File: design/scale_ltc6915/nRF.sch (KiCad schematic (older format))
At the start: 31 parts, among them J1 USB_B_Micro, J2 Conn_02x03_Odd_Even, J4 Conn_01x04, Q1 IRLML6401, SW1 SW_SPST, SW2 ON/OFF switch, U1 MDBT42Q, U2 BQ21040, U3 TPS7A0233PDBV, Y1 Q13FC1350000400

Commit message: BOMs, schematics updated, scale_ltc6915 PCB Design complete.
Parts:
- added Q3: AO3400, Package_TO_SOT_SMD:SOT-23, symbol Device:Q_NMOS_DGS
- added R10, R11: 10k, Resistor_SMD:R_0603_1608Metric_Pad1.05x0.95mm_HandSolder, symbol sense:R
- J4: footprint Connector_PinHeader_2.00mm:PinHeader_1x04_P2.00mm_Vertical -> Connector_PinHeader_2.00mm:PinHeader_1x02_P2.00mm_Vertical; symbol Connector_Generic:Conn_01x04 -> Connector_Generic:Conn_01x02
- U3: symbol scale_ltc6915.pro-rescue:TLV70013_SOT23-5-Regulator_Linear -> scale_ltc6915-rescue:TLV70013_SOT23-5-Regulator_Linear
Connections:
- net 10V_LDO_EN: now also U1.23 (P0.10/NFC2); no longer U1.16 (P0.03/AIN1)
- net BOOST_EN: now also U1.22 (P0.09/NFC1); no longer U1.17 (P0.04/AIN2)
- net BUTTON: now also U1.28 (TRACE_DATA3/P0.14); no longer U1.19 (P0.06)
- net CLK_nRF: now also U1.33 (P0.19); no longer U1.25 (P0.11)
- net CS1_nRF: now also U1.31 (P0.17); no longer U1.26 (P0.12)
- net CS2_nRF: now also U1.26 (P0.12); no longer U1.29 (TRACE_DATA2/P0.15)
- net EN_nRF: now also U1.29 (TRACE_DATA2/P0.15); no longer U1.21 (P0.08)
- net GND: now also Q3.3 (S)
- net GPIO0: now also U1.19 (P0.06); no longer U1.33 (P0.19)
- net GPIO1: now also U1.20 (P0.07); no longer U1.32 (TRACE_DATA0/P0.18)
- net MISO_nRF: now also U1.27 (P0.13); no longer U1.28 (TRACE_DATA3/P0.14)
- net MOSI_nRF: now also U1.32 (TRACE_DATA0/P0.18); no longer U1.20 (P0.07)
- net SHDW_nRF: now also U1.30 (TRACE_DATA1/P0.16); no longer U1.27 (P0.13)
- net VBAT: now also R10.2
- net Vlc: now also U1.17 (P0.04/AIN2); no longer U1.18 (P0.05/AIN3)
- removed net GPIO2: J4.3 (Pin_3), U1.31 (P0.17)
- removed net GPIO3: J4.4 (Pin_4), U1.30 (TRACE_DATA1/P0.16)
- new net: Q3.1 (D), R11.1
- new net BAT_LVL: R10.1, R11.2, U1.18 (P0.05/AIN3)
- new net BT_LVL_EN: Q3.2 (G), U1.21 (P0.08)
- no-connect marks 13 -> 12
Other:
- moved on the sheet: C16, SW1
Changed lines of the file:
@@
 L sense:GND #PWR01
 U 1 1 5A8704B4
-P 8770 3120
-F 0 "#PWR01" H 8770 2870 50  0001 C CNN
-F 1 "GND" H 8770 2970 50  0000 C CNN
-F 2 "" H 8770 3120 60  0000 C CNN
-F 3 "" H 8770 3120 60  0000 C CNN
-	1    8770 3120
+P 9320 5800
+F 0 "#PWR01" H 9320 5550 50  0001 C CNN
+F 1 "GND" H 9320 5650 50  0000 C CNN
+F 2 "" H 9320 5800 60  0000 C CNN
+F 3 "" H 9320 5800 60  0000 C CNN
+	1    9320 5800
 	1    0    0    -1
 $EndComp
@@
 Text Notes 6450 1100 0    60   ~ 0
 Reverse polarity protection
-Text Notes 8760 2445 0    60   ~ 0
+Text Notes 9310 5125 0    60   ~ 0
 Button for Tare
 Text Notes 1180 3310 0    60   ~ 0
@@
 L sense:C C16
 U 1 1 5D422270
-P 9510 2900
-F 0 "C16" H 9360 2995 50  0000 L CNN
-F 1 "0.1nF" H 9265 2820 50  0000 L CNN
-F 2 "sense_fp:C_0402_1005Metric" H 9548 2750 30  0001 C CNN
-F 3 "" H 9510 2900 60  0000 C CNN
-	1    9510 2900
+P 10060 5580
+F 0 "C16" H 9910 5675 50  0000 L CNN
+F 1 "0.1nF" H 9815 5500 50  0000 L CNN
+F 2 "sense_fp:C_0402_1005Metric" H 10098 5430 30  0001 C CNN
+F 3 "" H 10060 5580 60  0000 C CNN
+	1    10060 5580
 	-1   0    0    1
 $EndComp
@@
 L sense:GND #PWR032
 U 1 1 5D42FC1A
-P 9510 3110
-F 0 "#PWR032" H 9510 2860 50  0001 C CNN
-F 1 "GND" H 9510 2960 50  0000 C CNN
-F 2 "" H 9510 3110 60  0000 C CNN
-F 3 "" H 9510 3110 60  0000 C CNN
-	1    9510 3110
+P 10060 5790
+F 0 "#PWR032" H 10060 5540 50  0001 C CNN
+F 1 "GND" H 10060 5640 50  0000 C CNN
+F 2 "" H 10060 5790 60  0000 C CNN
+F 3 "" H 10060 5790 60  0000 C CNN
+	1    10060 5790
 	1    0    0    -1
 $EndComp
@@
 L sense:SW_SPST SW1
 U 1 1 5E71D3F6
-P 9160 2640
-F 0 "SW1" H 9160 2765 50  0000 C CNN
-F 1 "SW_SPST" H 9160 2540 50  0000 C CNN
-F 2 "Footprint_nrf_scale:SMD Tactile Switch_3x6x2.5mm" H 9160 2640 50  0001 C CNN
-F 3 "" H 9160 2640 50  0001 C CNN
-	1    9160 2640
+P 9710 5320
+F 0 "SW1" H 9710 5445 50  0000 C CNN
+F 1 "SW_SPST" H 9710 5220 50  0000 C CNN
+F 2 "Footprint_nrf_scale:SMD Tactile Switch_3x6x2.5mm" H 9710 5320 50  0001 C CNN
+F 3 "" H 9710 5320 50  0001 C CNN
+	1    9710 5320
 	1    0    0    -1
 $EndComp
@@
 Wire Wire Line
 	7220 4000 7800 4000
-Text Label 10150 2640 2    50   ~ 0
+Text Label 10700 5320 2    50   ~ 0
 BUTTON
 Wire Wire Line
-	9510 3050 9510 3110
-Wire Wire Line
-	8770 3120 8770 2640
-Wire Wire Line
-	8770 2640 8960 2640
-Wire Wire Line
-	9360 2640 9510 2640
-Wire Wire Line
-	9510 2750 9510 2640
-Connection ~ 9510 2640
-Wire Wire Line
-	9510 2640 10150 2640
+	10060 5730 10060 5790
+Wire Wire Line
+	9320 5800 9320 5320
+Wire Wire Line
+	9320 5320 9510 5320
+Wire Wire Line
+	9910 5320 10060 5320
+Wire Wire Line
+	10060 5430 10060 5320
+Connection ~ 10060 5320
+Wire Wire Line
+	10060 5320 10700 5320
 $Comp
 L sense:Battery_Cell BT1
@@
 VBAT
 $Comp
-L scale_ltc6915.pro-rescue:TLV70013_SOT23-5-Regulator_Linear U?
+L scale_ltc6915-rescue:TLV70013_SOT23-5-Regulator_Linear U?
 U 1 1 5E60E4CD
 P 9300 1450
@@
 Text HLabel 7550 1350 2    50   Output ~ 0
 VBAT
-Text Label 6120 6300 1    50   ~ 0
+Text Label 7800 4600 2    50   ~ 0
 BUTTON
 Wire Wire Line
-	6020 6300 6020 5650
-Wire Wire Line
-	6120 5650 6120 6300
-NoConn ~ 6420 5650
-NoConn ~ 6520 5650
+	6220 6300 6220 5650
+Wire Wire Line
+	6320 5650 6320 6300
 Wire Wire Line
 	7800 4900 7220 4900
@@
 NoConn ~ 5720 5650
 Wire Wire Line
-	6220 5650 6220 6300
-Wire Wire Line
-	6320 5650 6320 6300
+	6420 5650 6420 6300
+Wire Wire Line
+	6520 5650 6520 6300
 NoConn ~ 7220 3600
 $Comp
-L Connector_Generic:Conn_01x04 J4
+L Connector_Generic:Conn_01x02 J4
 U 1 1 5E6691E5
-P 10400 4450
-F 0 "J4" H 10480 4442 50  0000 L CNN
-F 1 "Conn_01x04" H 10480 4351 50  0000 L CNN
-F 2 "Connector_PinHeader_2.00mm:PinHeader_1x04_P2.00mm_Vertical" H 10400 4450 50  0001 C CNN
-F 3 "~" H 10400 4450 50  0001 C CNN
-	1    10400 4450
-	1    0    0    -1
-$EndComp
-Text Label 9900 4350 0    50   ~ 0
+P 10360 4100
+F 0 "J4" H 10440 4092 50  0000 L CNN
+F 1 "Conn_01x04" H 10440 4001 50  0000 L CNN
+F 2 "Connector_PinHeader_2.00mm:PinHeader_1x02_P2.00mm_Vertical" H 10360 4100 50  0001 C CNN
+F 3 "~" H 10360 4100 50  0001 C CNN
+	1    10360 4100
+	1    0    0    -1
+$EndComp
+Text Label 9860 4100 0    50   ~ 0
 GPIO0
-Text Label 9900 4450 0    50   ~ 0
+Text Label 9860 4200 0    50   ~ 0
 GPIO1
-Text Label 9900 4550 0    50   ~ 0
-GPIO2
-Text Label 9900 4650 0    50   ~ 0
-GPIO3
-Wire Wire Line
-	9900 4650 10200 4650
-Wire Wire Line
-	10200 4550 9900 4550
-Wire Wire Line
-	9900 4450 10200 4450
-Wire Wire Line
-	10200 4350 9900 4350
-Text Label 7800 4100 2    50   ~ 0
+Wire Wire Line
+	9860 4200 10160 4200
+Wire Wire Line
+	10160 4100 9860 4100
+Text Label 6120 6300 1    50   ~ 0
 GPIO0
-Text Label 7800 4200 2    50   ~ 0
+Text Label 6220 6300 1    50   ~ 0
 GPIO1
-Text Label 7800 4300 2    50   ~ 0
-GPIO2
-Text Label 7800 4400 2    50   ~ 0
-GPIO3
 Wire Wire Line
 	7220 4400 7800 4400
@@
 Wire Wire Line
 	7800 4300 7220 4300
-Text HLabel 5920 6300 3    50   Output ~ 0
+Text HLabel 6420 6300 3    50   Output ~ 0
 BOOST_EN
-Text HLabel 5820 6300 3    50   Output ~ 0
+Text HLabel 6520 6300 3    50   Output ~ 0
 10V_LDO_EN
-Text HLabel 6020 6300 3    50   Input ~ 0
+Text HLabel 5920 6300 3    50   Input ~ 0
 Vlc
+Text HLabel 7800 4400 2    50   Output ~ 0
+SHDW_nRF
+Text HLabel 7800 4300 2    50   Output ~ 0
+CS1_nRF
+Text HLabel 7800 4200 2    50   Output ~ 0
+MOSI_nRF
+Text HLabel 7800 4100 2    50   Output ~ 0
+CLK_nRF
+Text HLabel 7800 4800 2    50   Output ~ 0
+CS2_nRF
 Text HLabel 7800 4700 2    50   Output ~ 0
-SHDW_nRF
-Text HLabel 7800 4800 2    50   Output ~ 0
-CS1_nRF
-Text HLabel 6220 6300 3    50   Output ~ 0
-MOSI_nRF
-Text HLabel 7800 4900 2    50   Output ~ 0
-CLK_nRF
+MISO_nRF
 Text HLabel 7800 4500 2    50   Output ~ 0
-CS2_nRF
-Text HLabel 7800 4600 2    50   Output ~ 0
-MISO_nRF
-Text HLabel 6320 6300 3    50   Output ~ 0
 EN_nRF
 Wire Wire Line
-	5820 6300 5820 5650
+	6020 6300 6020 5650
+Wire Wire Line
+	6120 5650 6120 6300
+Wire Wire Line
+	7800 4500 7220 4500
+Wire Wire Line
+	7220 4600 7800 4600
+Text Label 10440 2110 2    50   ~ 0
+VBAT
+$Comp
+L Device:Q_NMOS_DGS Q3
+U 1 1 5E6E2B83
+P 10340 3310
+F 0 "Q3" H 10544 3356 50  0000 L CNN
+F 1 "AO3400" H 10544 3265 50  0000 L CNN
+F 2 "Package_TO_SOT_SMD:SOT-23" H 10540 3410 50  0001 C CNN
+F 3 "~" H 10340 3310 50  0001 C CNN
+	1    10340 3310
+	1    0    0    -1
+$EndComp
+$Comp
+L sense:R R10
+U 1 1 5E6E3BA3
+P 10440 2350
+F 0 "R10" V 10340 2350 50  0000 C CNN
+F 1 "10k" V 10440 2350 50  0000 C CNN
+F 2 "Resistor_SMD:R_0603_1608Metric_Pad1.05x0.95mm_HandSolder" V 10370 2350 50  0001 C CNN
+F 3 "" H 10440 2350 50  0001 C CNN
+	1    10440 2350
+	-1   0    0    1
+$EndComp
+$Comp
+L sense:R R11
+U 1 1 5E6E57D8
+P 10440 2860
+F 0 "R11" V 10340 2860 50  0000 C CNN
+F 1 "10k" V 10440 2860 50  0000 C CNN
+F 2 "Resistor_SMD:R_0603_1608Metric_Pad1.05x0.95mm_HandSolder" V 10370 2860 50  0001 C CNN
+F 3 "" H 10440 2860 50  0001 C CNN
+	1    10440 2860
+	-1   0    0    1
+$EndComp
+$Comp
+L sense:GND #PWR0128
+U 1 1 5E6F8C54
+P 10440 3620
+F 0 "#PWR0128" H 10440 3370 50  0001 C CNN
+F 1 "GND" H 10440 3470 50  0000 C CNN
+F 2 "" H 10440 3620 60  0000 C CNN
+F 3 "" H 10440 3620 60  0000 C CNN
+	1    10440 3620
+	1    0    0    -1
+$EndComp
+Wire Wire Line
+	10440 3620 10440 3510
+Wire Wire Line
+	10440 3010 10440 3110
+Wire Wire Line
+	10440 2500 10440 2600
+Wire Wire Line
+	10440 2110 10440 2200
+Wire Wire Line
+	10140 3310 9750 3310
+Wire Wire Line
+	10440 2600 9750 2600
+Connection ~ 10440 2600
+Wire Wire Line
+	10440 2600 10440 2710
+Text Label 9750 2600 0    50   ~ 0
+BAT_LVL
+Text Label 9750 3310 0    50   ~ 0
+BT_LVL_EN
+Text Label 6020 6300 1    50   ~ 0
+BAT_LVL
+Text Label 6320 6300 1    50   ~ 0
+BT_LVL_EN
 Wire Wire Line
 	5920 5650 5920 6300
-Wire Wire Line
-	7800 4500 7220 4500
-Wire Wire Line
-	7220 4600 7800 4600
+NoConn ~ 5820 5650
 $EndSCHEMATC

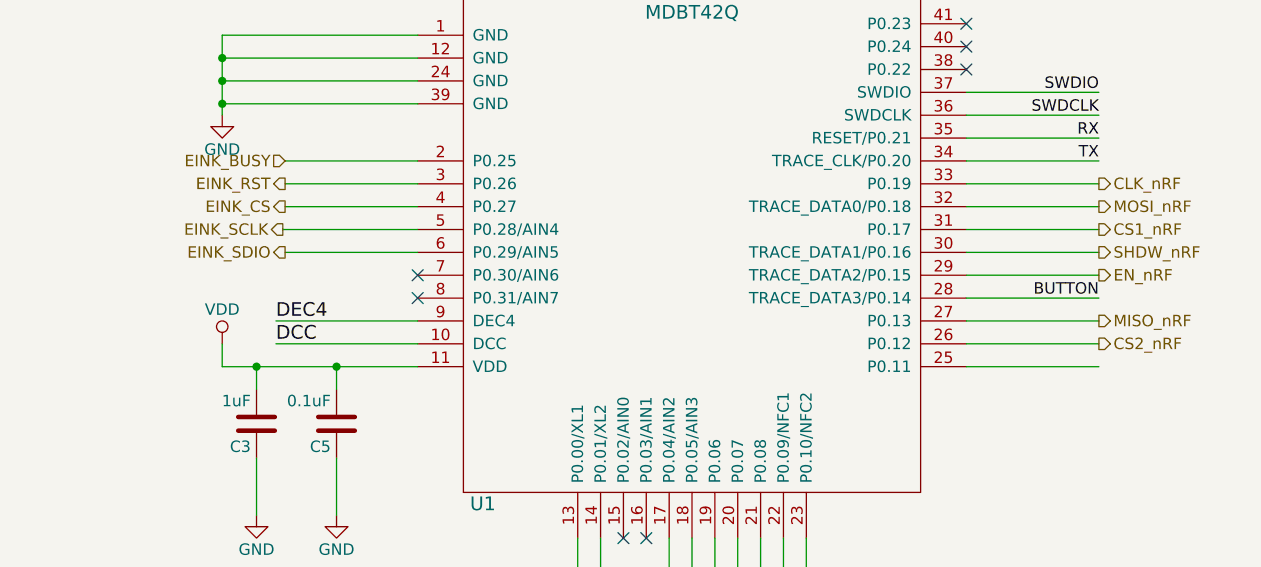
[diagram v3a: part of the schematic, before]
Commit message: DC, CS pins separated, issue fixed. In both scale_hx711 and scale_ltc6915.
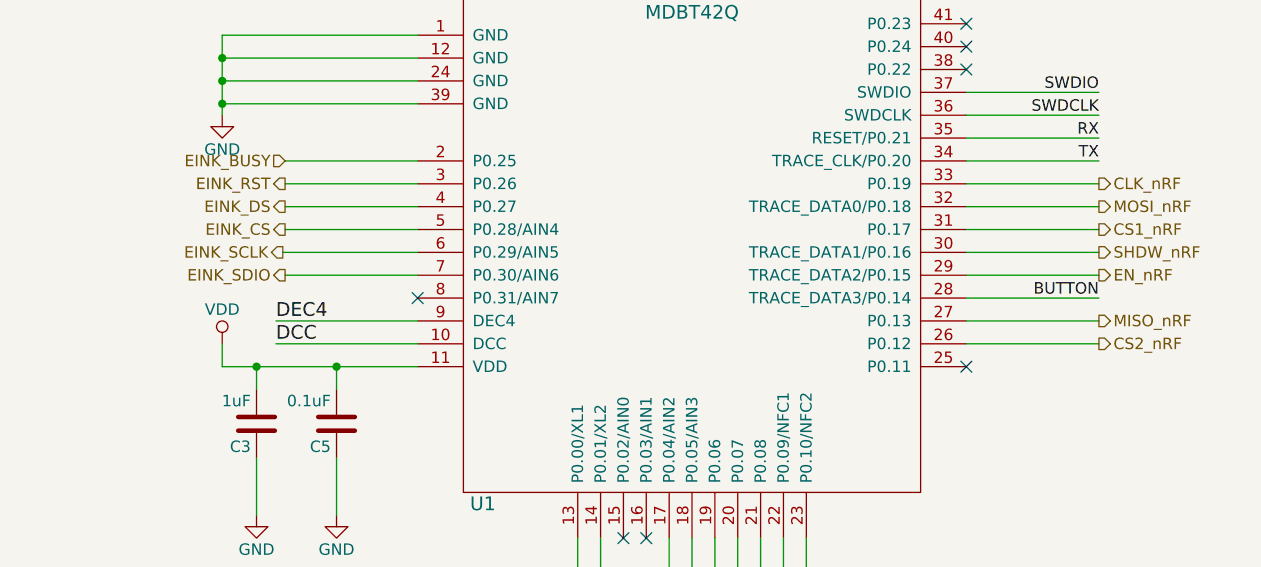
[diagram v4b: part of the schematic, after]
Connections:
- net EINK_CS: now also U1.5 (P0.28/AIN4); no longer U1.4 (P0.27)
- net EINK_SCLK: now also U1.6 (P0.29/AIN5); no longer U1.5 (P0.28/AIN4)
- net EINK_SDIO: now also U1.7 (P0.30/AIN6); no longer U1.6 (P0.29/AIN5)
- new net EINK_DS: U1.4 (P0.27)
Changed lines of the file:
@@
 	6320 5650 6320 6300
-Wire Wire Line
-	7800 4900 7220 4900
 Wire Wire Line
 	7220 4800 7800 4800
 Wire Wire Line
 	7800 4700 7220 4700
-Text HLabel 4240 4400 0    50   Output ~ 0
+Text HLabel 4240 4500 0    50   Output ~ 0
 EINK_SDIO
-Text HLabel 4230 4300 0    50   Output ~ 0
+Text HLabel 4230 4400 0    50   Output ~ 0
 EINK_SCLK
-Text HLabel 4240 4200 0    50   Output ~ 0
+Text HLabel 4240 4300 0    50   Output ~ 0
 EINK_CS
 Text HLabel 4240 4100 0    50   Output ~ 0
@@
 	4240 4000 4820 4000
 Wire Wire Line
-	4820 4200 4240 4200
+	4820 4300 4240 4300
 Wire Wire Line
-	4820 4400 4240 4400
+	4820 4500 4240 4500
 Wire Wire Line
 	2801 6900 2801 6975
@@
 	2800 7075 2300 7075
 NoConn ~ 4820 4600
-NoConn ~ 4820 4500
 Wire Wire Line
 	4820 4100 4240 4100
 Wire Wire Line
-	4230 4300 4820 4300
+	4230 4400 4820 4400
 $Comp
 L sense:MDBT42Q U1
@@
 	5920 5650 5920 6300
 NoConn ~ 5820 5650
+NoConn ~ 7220 4900
+Text HLabel 4240 4200 0    50   Output ~ 0
+EINK_DS
+Wire Wire Line
+	4820 4200 4240 4200
 $EndSCHEMATC
